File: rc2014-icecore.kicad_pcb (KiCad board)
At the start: 2 copper layers, 99.3 x 60.1 mm, 21 parts, among them J1 Conn_01x39, J2 Conn_01x10, J3 Conn_02x15_Odd_Even, J4 Conn_02x13_Odd_Even, U1 LM1117-3.3, U2 SN74CB3T3245, U3 SN74CB3T3245, U4 SN74CB3T3245, U5 SN74CB3T3245, U6 SN74CB3T3245

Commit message: WIP of level shifter
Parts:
- removed A1: BE-CARRIER, blackedge:BE-CARRIER-SMD
- removed H1: MountingHole, MountingHole:MountingHole_3.2mm_M3
- removed J4: Conn_02x13_Odd_Even, Connector_PinHeader_2.54mm:PinHeader_2x13_P2.54mm_Horizontal
- added JP2: Jumper, Connector_PinHeader_2.54mm:PinHeader_1x02_P2.54mm_Vertical, F.Cu at (134.1, 145.7)
- added REF**: OSHW-Symbol_6.7x6mm_SilkScreen, Symbol:OSHW-Symbol_6.7x6mm_SilkScreen, B.Cu at (152.4, 155.2)
- J3: value Conn_02x15_Odd_Even -> Conn_02x25_Odd_Even; footprint Connector_PinSocket_2.54mm:PinSocket_2x15_P2.54mm_Horizontal -> Connector_PinSocket_2.54mm:PinSocket_2x25_P2.54mm_Vertical
- moved JP1 76.4 mm to (143.3, 151.5)
- moved J3 61.3 mm to (65.5, 143.6), turned to 90 degrees
- moved C1 54.3 mm to (147.6, 152.1)
- moved C2 54.3 mm to (156.8, 152.1)
- moved U1 54.3 mm to (152.1, 154.5)
- moved R1 38.8 mm to (65.3, 156.2)
- moved U2 30.4 mm to (70.2, 153.9)
- moved C4 30.3 mm to (65.4, 151.9)
- moved U3 28.7 mm to (86.5, 153.9)
- moved C5 28.7 mm to (81.7, 151.9)
- moved U5 28.3 mm to (119.8, 153.9)
- moved C7 28.3 mm to (114.9, 151.9)
- moved U4 28.0 mm to (103.0, 153.9)
- moved C6 28.0 mm to (98.2, 151.9)
- moved C3 20.2 mm to (131.3, 151.9)
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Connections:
- J2 pad 8: (no net) -> /~BUSREQ
- J3 pad 1: +3V3 -> /P0
- J3 pad 10: /P36 -> /P9
- J3 pad 11: /P39 -> /P10
- J3 pad 12: /P37 -> /P11
- J3 pad 13: /AN9 -> /P12
- J3 pad 14: /AN8 -> /P13
- J3 pad 15: +5V -> /P14
- J3 pad 16: /AN7 -> /P15
- J3 pad 17: /AN6 -> (no net)
- J3 pad 18: /AN5 -> /P17
- J3 pad 19: +3V3 -> /P18
- J3 pad 2: +3V3 -> /P1
- J3 pad 20: +3V3 -> /P19
- J3 pad 21: GND -> /P20
- J3 pad 22: GND -> /P21
- J3 pad 23: /P42 -> /P22
- J3 pad 24: /P46 -> /P23
- J3 pad 25: /P43 -> /P24
- J3 pad 26: /P47 -> /P25
- J3 pad 27: /P40 -> /P26
- J3 pad 28: /P44 -> /P27
- J3 pad 29: /P41 -> /P28
- J3 pad 3: GND -> /P2
- J3 pad 30: /P45 -> /P29
- J3 pad 4: GND -> /P3
- J3 pad 5: /P34 -> /P4
- J3 pad 6: /P32 -> /P5
- J3 pad 7: /P35 -> /P6
- J3 pad 8: /P33 -> /P7
- J3 pad 9: /P38 -> /P8
- U2 pad 11: /P8 -> /P7
- U2 pad 14: /P3 -> /P4
- U2 pad 15: /P4 -> /P3
- U3 pad 14: /P11 -> /P12
- U3 pad 15: /P12 -> /P11
- U3 pad 18: /P7 -> /P8
- U4 pad 11: /P21 -> /P22
- U4 pad 12: /P22 -> /P21
- U4 pad 15: /P17 -> /P18
- U4 pad 16: /P18 -> /P17
- U4 pad 17: /P16 -> GND
- U4 pad 18: (no net) -> GND
- U4 pad 2: (no net) -> GND
- U4 pad 3: (no net) -> GND
- U5 pad 12: /P29 -> /P30
- U5 pad 13: /P30 -> /P29
- U5 pad 16: /P25 -> /P26
- U5 pad 17: /P26 -> /P25
- U5 pad 5: (no net) -> /~BUSREQ
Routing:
- net GND: track 257.3 -> 51.0 mm, vias 0 -> 14
- net +3V3: track 188.6 -> 100.5 mm, vias 1 -> 0
- net /P32: track 48.4 -> 0.00 mm
- net /TDI: track 46.2 -> 0.00 mm, vias 1 -> 0
- net /TCK: track 45.8 -> 0.00 mm, vias 1 -> 0
- net /TDO: track 45.7 -> 0.00 mm, vias 1 -> 0
- net /AN5: track 45.4 -> 0.00 mm, vias 1 -> 0
- net /P33: track 45.1 -> 0.00 mm
- net /A4: track 50.6 -> 7.99 mm
- net /P34: track 42.5 -> 0.00 mm
- net /P36: track 42.0 -> 0.00 mm
- net /A5: track 48.6 -> 7.20 mm
- net /AN7: track 41.2 -> 0.00 mm, vias 1 -> 0
- net /TMS: track 40.5 -> 0.00 mm, vias 1 -> 0
- net /AN6: track 40.0 -> 0.00 mm, vias 1 -> 0
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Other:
- board size 99.3 x 60.1 mm -> 99.3 x 22.4 mm
- board text added: "SN74CB3T3245 FPGA Level Translator"
- board text removed: "3.3V source"
- board text removed: "FPGA"
- board text removed: "RC2014 IceCore Interface"
- board text removed: "Reg"
- board text removed: "github.com/electrified/rc2014-fpga-interface"

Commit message: Rev 1 as sent to JLCPCB
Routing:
- net GND: track 51.0 -> 49.8 mm

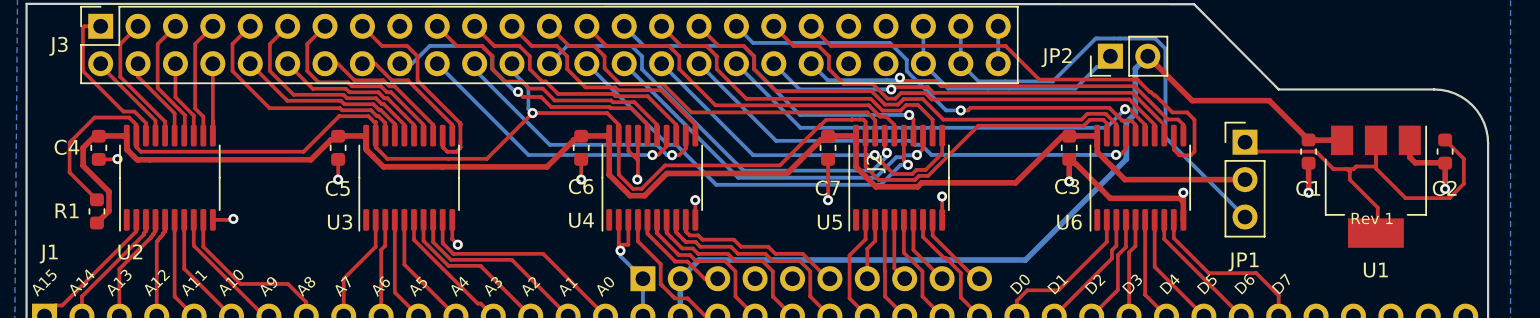
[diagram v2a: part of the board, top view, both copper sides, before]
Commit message: Update for Kicad 6
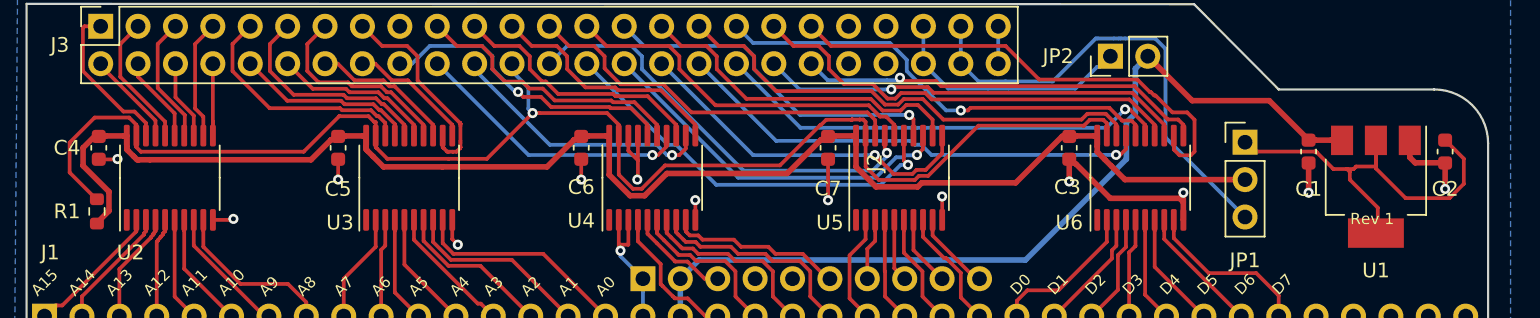
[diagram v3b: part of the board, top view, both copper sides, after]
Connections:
- net /~BUSREQ renamed /~{BUSREQ}
- net /~HALT renamed /~{HALT}
- net /~NMI renamed /~{NMI}
- net /~RFSH renamed /~{RFSH}
- net /~WAIT renamed /~{WAIT}
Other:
- net class Default removed
- net class IO removed
- net class Power removed
